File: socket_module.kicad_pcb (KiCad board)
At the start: 2 copper layers, 257 x 204.5 mm, 127 parts, among them J1 DIN41612_03x32_ABC, J2 DIN41612_03x32_ABC, Q1 RFD14N05L, Q10 RFD14N05L, Q11 RFD14N05L, Q12 RFD14N05L, Q13 RFD14N05L, Q14 RFD14N05L, Q15 RFD14N05L, Q16 RFD14N05L, Q17 RFD14N05L, Q18 RFD14N05L, Q19 RFD14N05L, Q2 RFD14N05L, Q20 RFD14N05L, Q21 RFD14N05L, Q22 RFD14N05L, Q23 RFD14N05L, Q24 RFD14N05L, Q25 RFD14N05L, Q26 RFD14N05L, Q27 RFD14N05L, Q28 RFD14N05L, Q29 RFD14N05L, Q3 RFD14N05L, Q30 RFD14N05L, Q31 RFD14N05L, Q32 RFD14N05L, Q33 RFD14N05L, Q34 RFD14N05L, Q35 RFD14N05L, Q36 RFD14N05L, Q37 RFD14N05L, Q38 RFD14N05L, Q39 RFD14N05L, Q4 RFD14N05L, Q40 RFD14N05L, Q41 RFD14N05L, Q42 RFD14N05L, Q43 RFD14N05L, Q44 RFD14N05L, Q45 RFD14N05L, Q46 RFD14N05L, Q47 RFD14N05L, Q48 RFD14N05L, Q5 RFD14N05L, Q6 RFD14N05L, Q7 RFD14N05L, Q8 RFD14N05L, Q9 RFD14N05L, U1 PAL22V10, U2 74HCTLS259, U3 74HCT244, U4 74HCTLS259, U5 74HCTLS259, U6 74HCTLS259, U7 74HCTLS259, U8 74HCTLS259

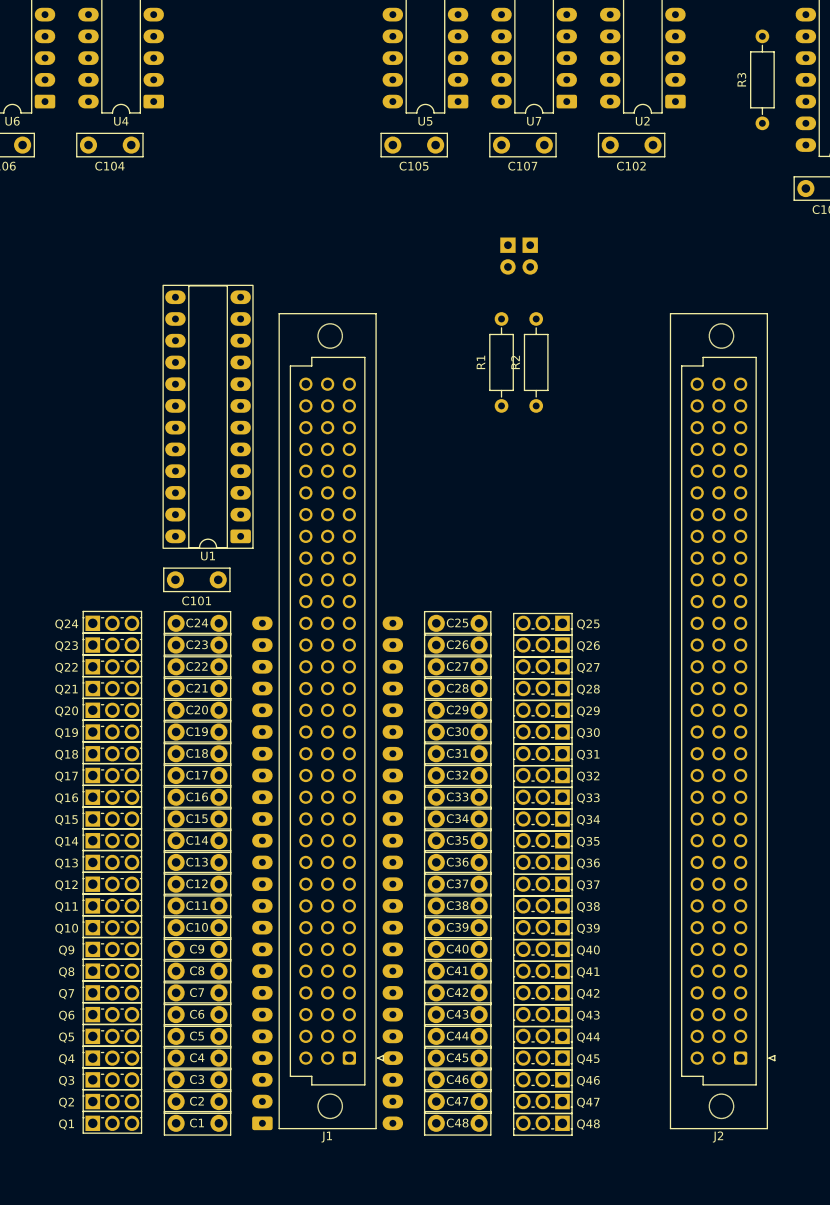
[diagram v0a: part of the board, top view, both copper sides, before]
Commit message: updates:
- update symbols and footprints from library
- re-correct 84 pin PLCC pin numbers
- reset transistors to TO-2whatever from SMD
- adjust position of DIN connectors, LEDs and their resistors (and 48 pin DIP and transistors and decoupling capacitors):  measured again.
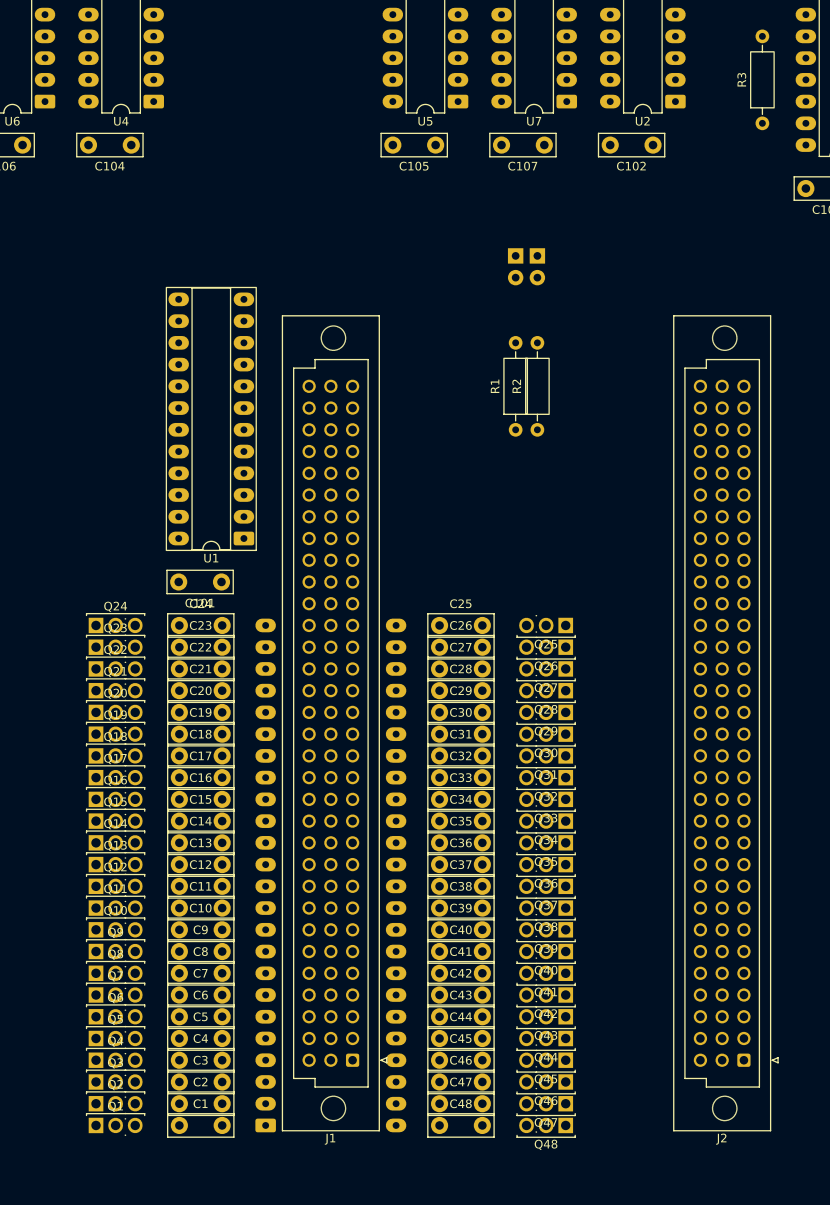
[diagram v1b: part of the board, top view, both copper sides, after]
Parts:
- PLCC20: value Conn_02x10_Counter_Clockwise -> Yamaichi IC120-0204-205
- PLCC28: value Conn_02x14_Counter_Clockwise -> Yamaichi IC120-0284-408
- PLCC32: value Conn_02x16_Counter_Clockwise -> Yamaichi IC120-0324-209
- PLCC44: value Conn_02x22_Counter_Clockwise -> Yamaichi IC120-0444-206
- PLCC52: value Conn_02x26_Counter_Clockwise -> Yamaichi IC120-0524-207
- PLCC68: value Conn_02x34_Counter_Clockwise -> Yamaichi IC120-0684-204
- PLCC84: value Conn_02x42_Row_Letter_First -> Yamaichi IC120-0844-203
- ZIF1: value Conn_02x24_Counter_Clockwise -> Aries 48-6554-10
- moved R1 3.24 mm to (198.8, 92.4)
- moved R2 2.79 mm to (201.4, 92.4)
- moved D1 1.54 mm to (198.8, 72.1)
- moved D2 1.51 mm to (201.4, 72.1)
- moved Q1 0.45 mm to (149.8, 173.7)
- moved Q10 0.45 mm to (149.8, 150.8)
- moved Q11 0.45 mm to (149.8, 148.3)
- moved Q12 0.45 mm to (149.8, 145.7)
- moved Q13 0.45 mm to (149.8, 143.2)
- moved Q14 0.45 mm to (149.8, 140.7)
- moved Q15 0.45 mm to (149.8, 138.1)
- moved Q16 0.45 mm to (149.8, 135.6)
- moved Q17 0.45 mm to (149.8, 133.0)
- moved Q18 0.45 mm to (149.8, 130.5)
- moved Q19 0.45 mm to (149.8, 128.0)
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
